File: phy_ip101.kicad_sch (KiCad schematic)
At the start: 36 parts, among them SW1 SW_Push, SW2 SW_Push, U3 ESP32-WROOM-32D, U4 IP101GRI

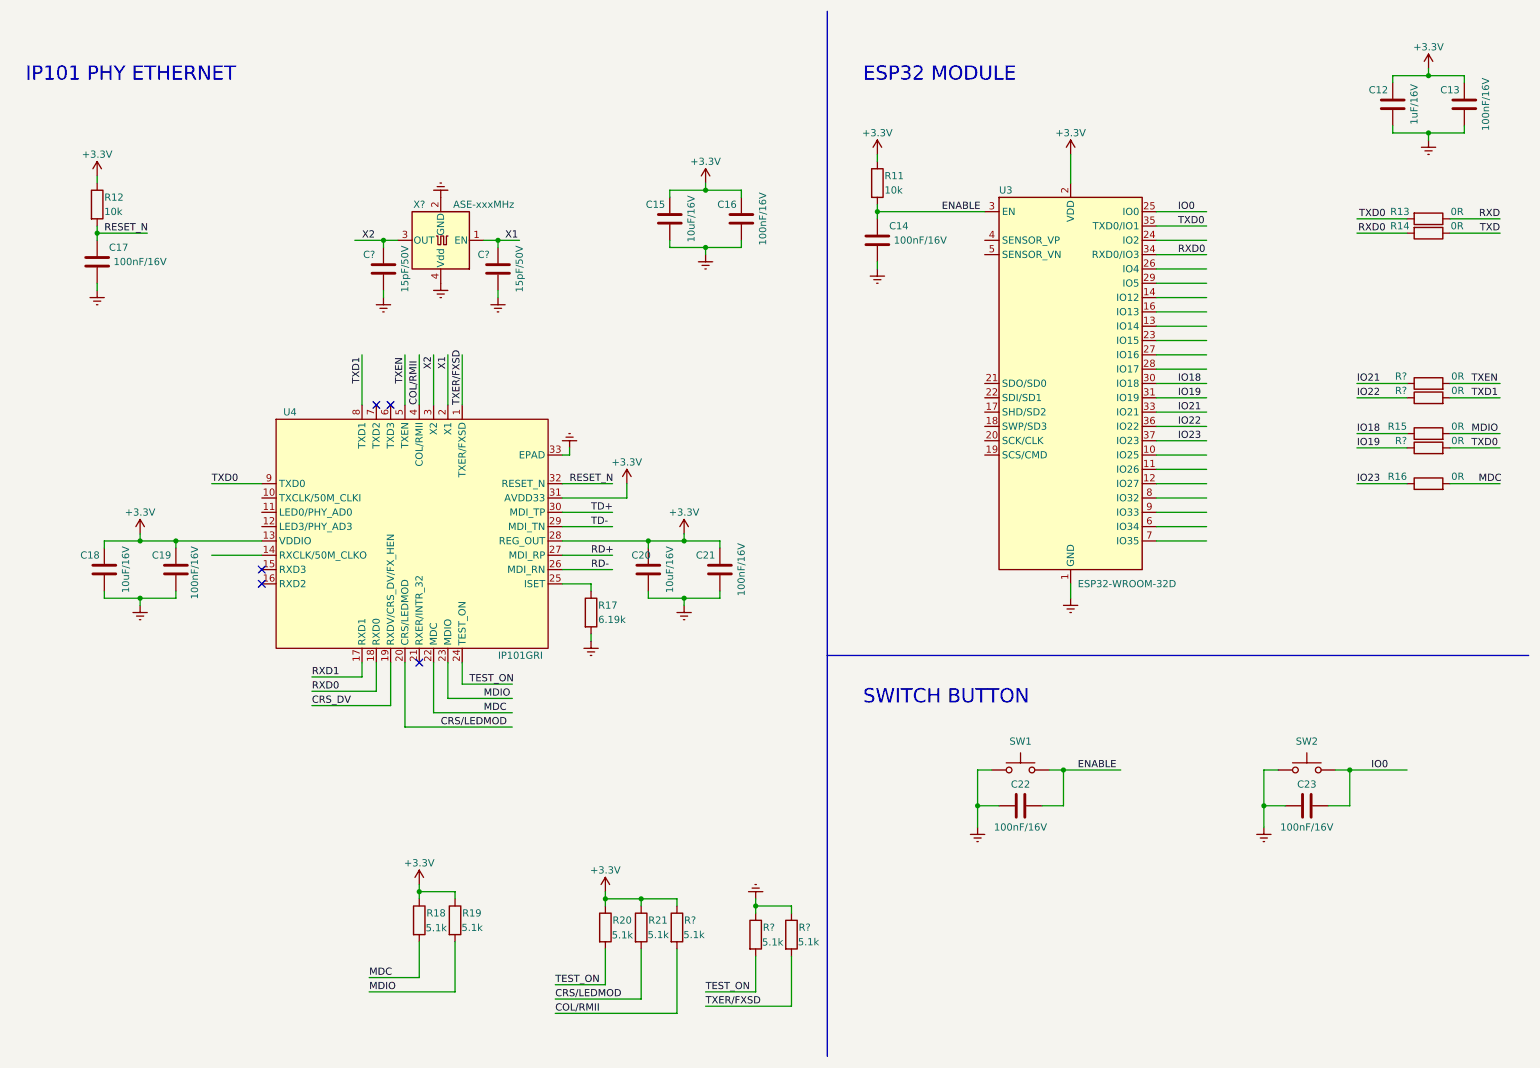
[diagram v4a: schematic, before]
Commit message: Concluido o circuito do PHY ETH
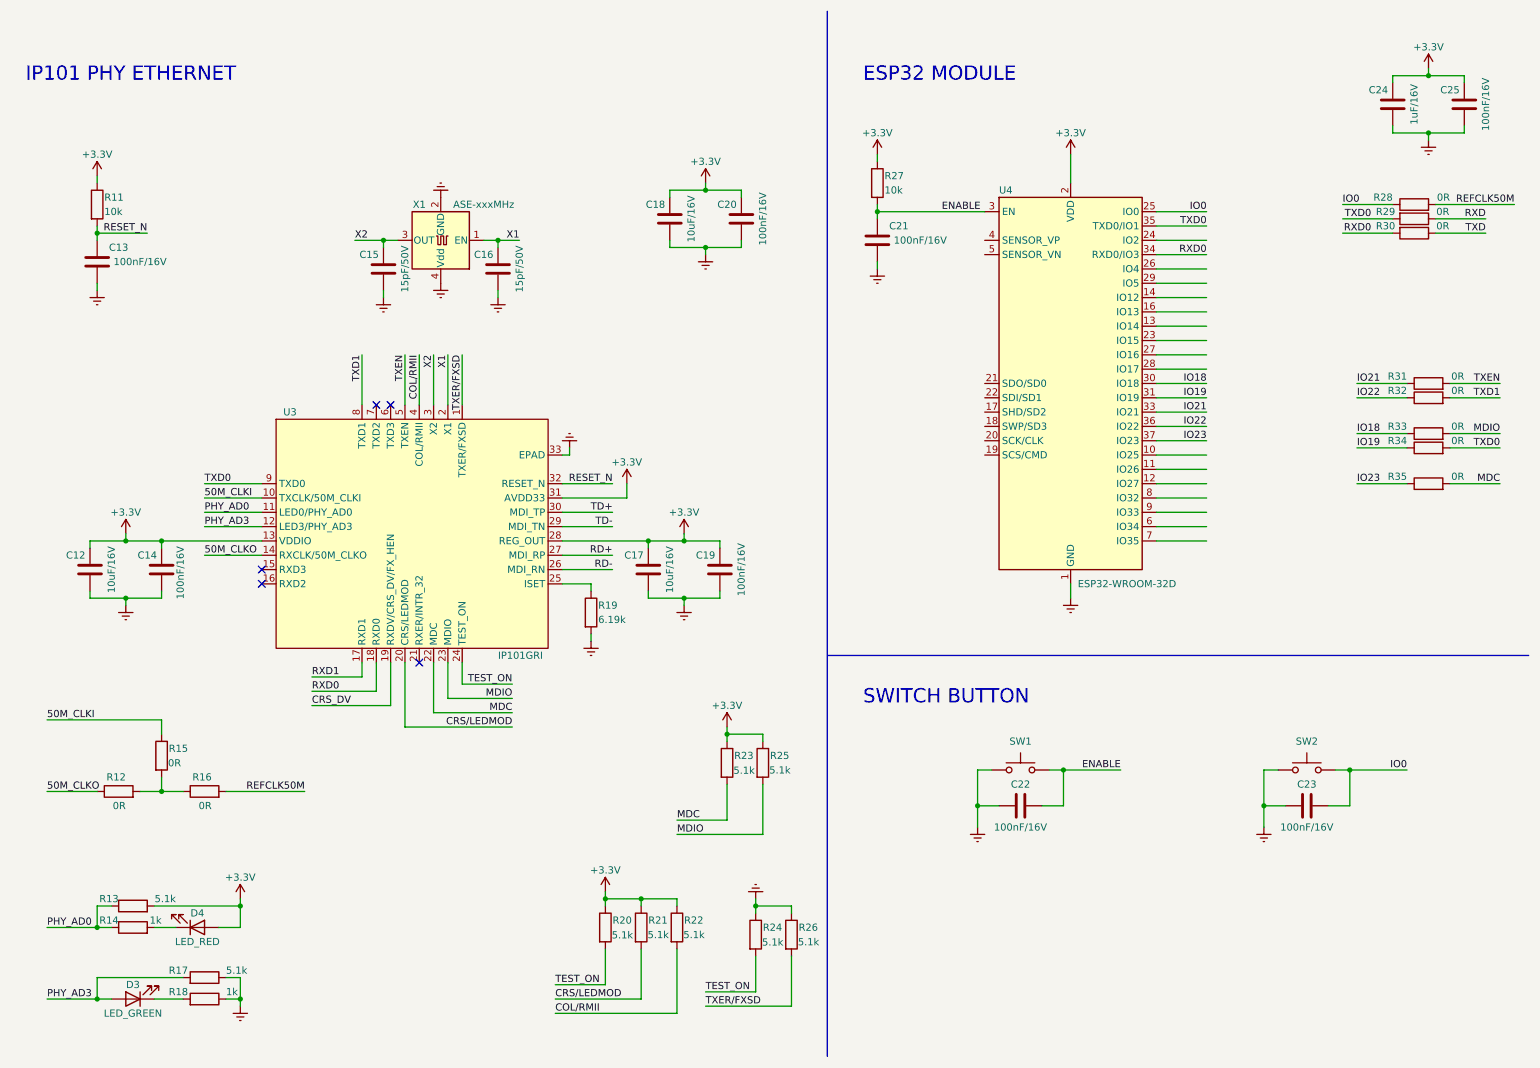
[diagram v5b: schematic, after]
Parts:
- added D3: LED_GREEN, LED_SMD:LED_0603_1608Metric_Pad1.05x0.95mm_HandSolder, symbol Device:LED
- added D4: LED_RED, LED_SMD:LED_0603_1608Metric_Pad1.05x0.95mm_HandSolder, symbol Device:LED
- added R12, R15, R16, R28: 0R, Resistor_SMD:R_0402_1005Metric_Pad0.72x0.64mm_HandSolder, symbol Device:R
- added R13, R17: 5.1k, Resistor_SMD:R_0402_1005Metric_Pad0.72x0.64mm_HandSolder, symbol Device:R
- added R14, R18: 1k, Resistor_SMD:R_0402_1005Metric_Pad0.72x0.64mm_HandSolder, symbol Device:R
- gave numbers to parts that had none: 9
- renumbered C18 to C12, C17 to C13, C19 to C14, C20 to C17, C15 to C18, C21 to C19, C16 to C20, C14 to C21, C12 to C24, C13 to C25, R12 to R11, R17 to R19, R18 to R23, R19 to R25, R11 to R27, R13 to R29, R14 to R30, R15 to R33, R16 to R35, U4 to U3, U3 to U4
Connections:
- net +3V3: now also D4.2 (A), R13.2
- net GNDREF: now also R17.1, R18.1
- net IO0: now also R28.1
- net 50M_CLKI: now reaches U3.10 (TXCLK/50M_CLKI)
- net 50M_CLKI: now also R15.1
- net PHY_AD0: now reaches U3.11 (LED0/PHY_AD0)
- net PHY_AD0: now also R13.1, R14.1
- net PHY_AD3: now reaches U3.12 (LED3/PHY_AD3)
- net PHY_AD3: now also D3.2 (A), R17.2
- net 50M_CLKO: now reaches U3.14 (RXCLK/50M_CLKO)
- net 50M_CLKO: now also R12.1
- new net: D4.1 (K), R14.2
- new net: R12.2, R15.2, R16.1
- new net: D3.1 (K), R18.2
- new net REFCLK50M: R16.2, R28.2
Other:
- moved on the sheet: C12, C14, R23, R25, R29, R30

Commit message: Iniciando o circuito do conector RJ45
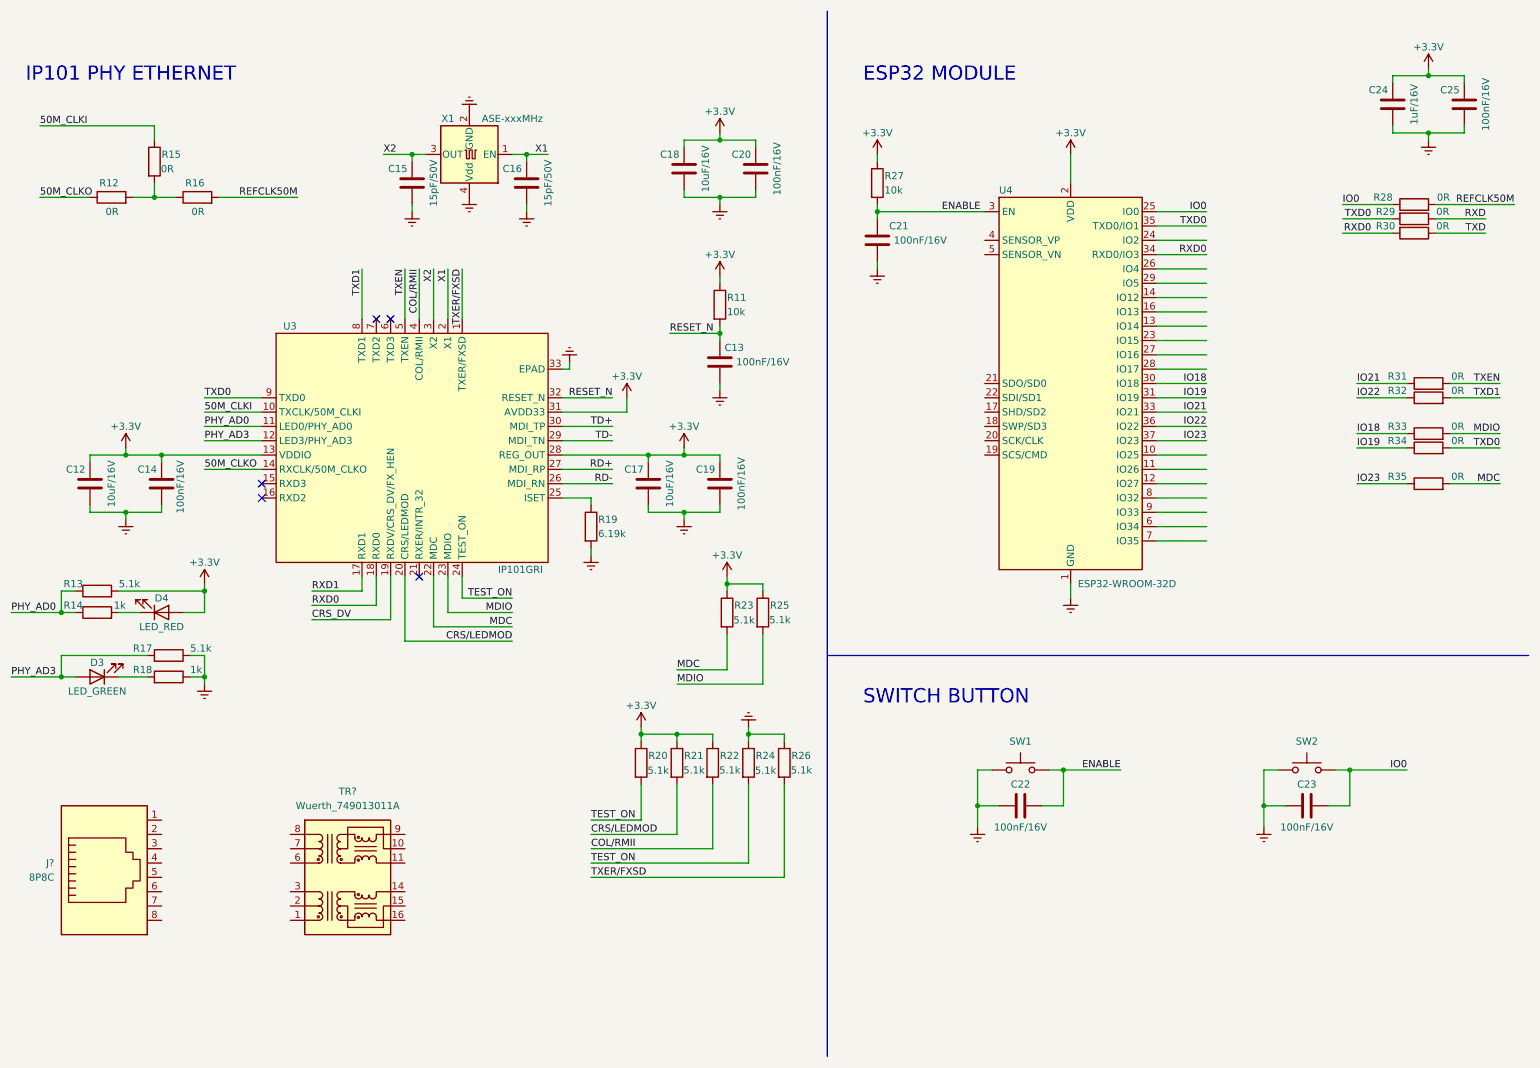
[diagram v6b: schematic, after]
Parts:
- added J?: 8P8C, Transformer_SMD:Transformer_Ethernet_YDS_30F-51NL_SO-24_7.1x15.1mm, symbol Connector:8P8C
- added TR?: Wuerth_749013011A, Transformer_SMD:Transformer_Ethernet_Wuerth_749013011A, symbol Transformer:Wuerth_749013011A
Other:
- moved on the sheet: C12, C13, C14, C15, C16, C17, C18, C19, C20, D3, D4, R11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

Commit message: Criado um sheet para circuito do ESP32
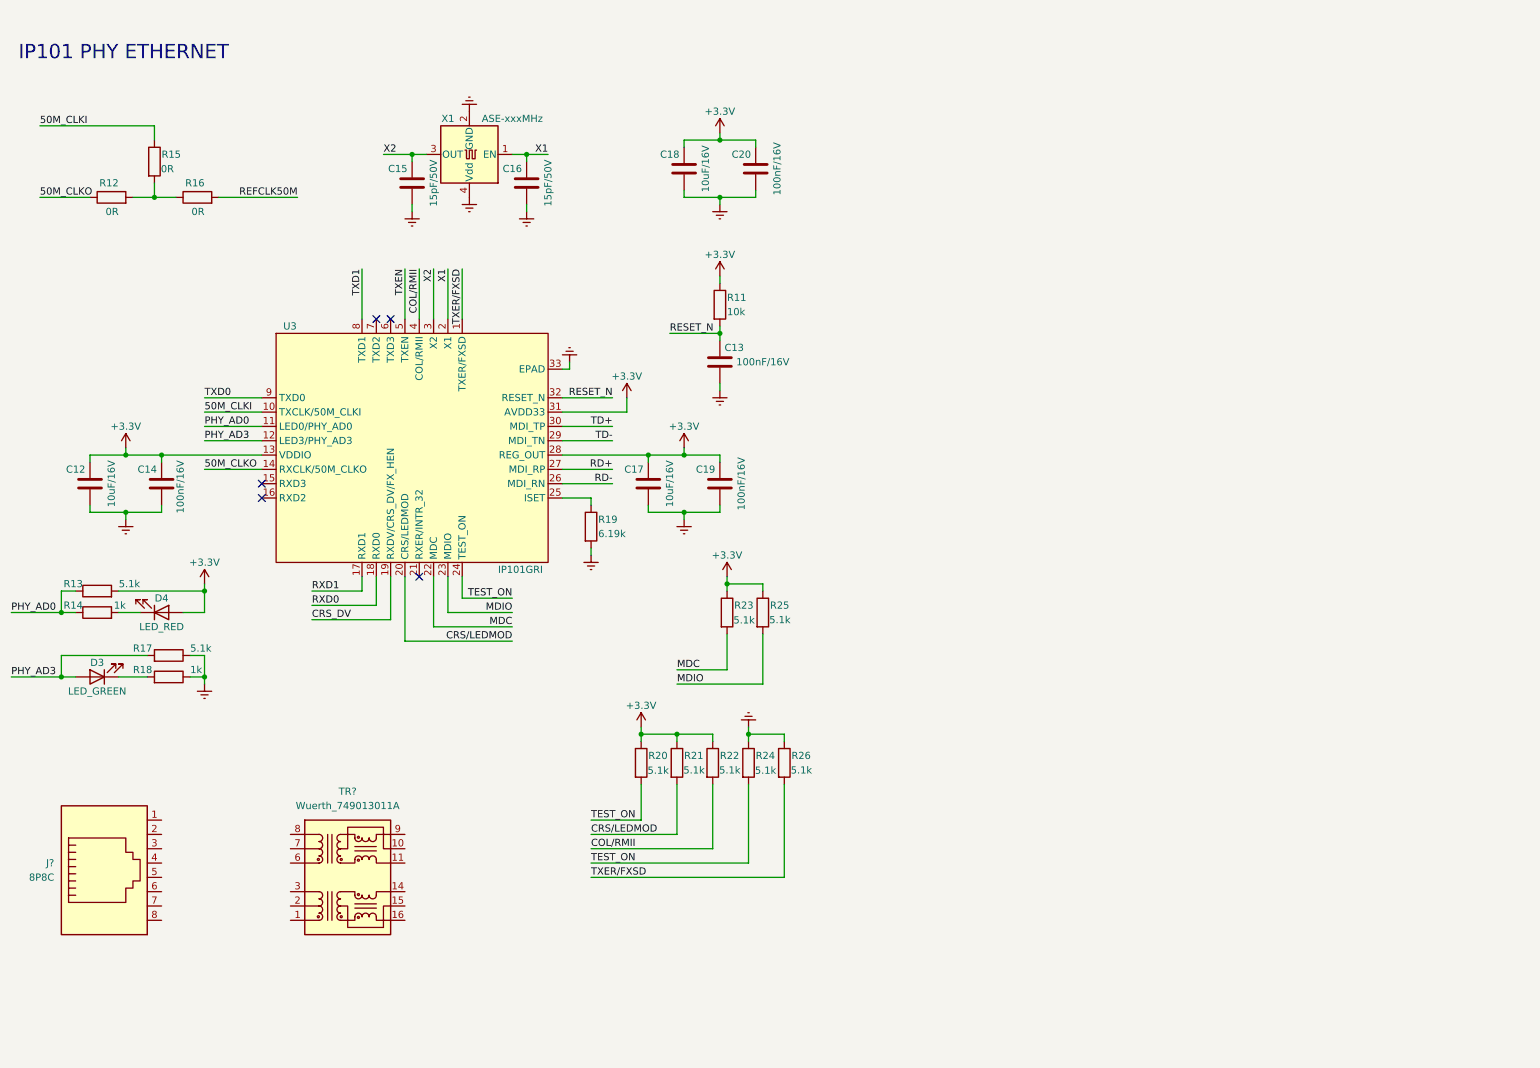
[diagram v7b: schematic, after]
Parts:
- removed C21, C22, C23, C25: 100nF/16V, Capacitor_SMD:C_0402_1005Metric_Pad0.74x0.62mm_HandSolder, symbol Device:C
- removed C24: 1uF/16V, Capacitor_SMD:C_0603_1608Metric_Pad1.08x0.95mm_HandSolder, symbol Device:C
- removed R27: 10k, symbol Device:R
- removed R28, R29, R30, R31, R32, R33, R34, R35: 0R, Resistor_SMD:R_0402_1005Metric_Pad0.72x0.64mm_HandSolder, symbol Device:R
- removed SW1, SW2: SW_Push, Button_Switch_SMD:SW_SPST_CK_RS282G05A3, symbol Switch:SW_Push
- removed U4: ESP32-WROOM-32D, RF_Module:ESP32-WROOM-32, symbol RF_Module:ESP32-WROOM-32D
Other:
- note removed: "ESP32 MODULE"
- note removed: "SWITCH BUTTON"

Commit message: Adicionado o circuito de entrada do PHY ETH
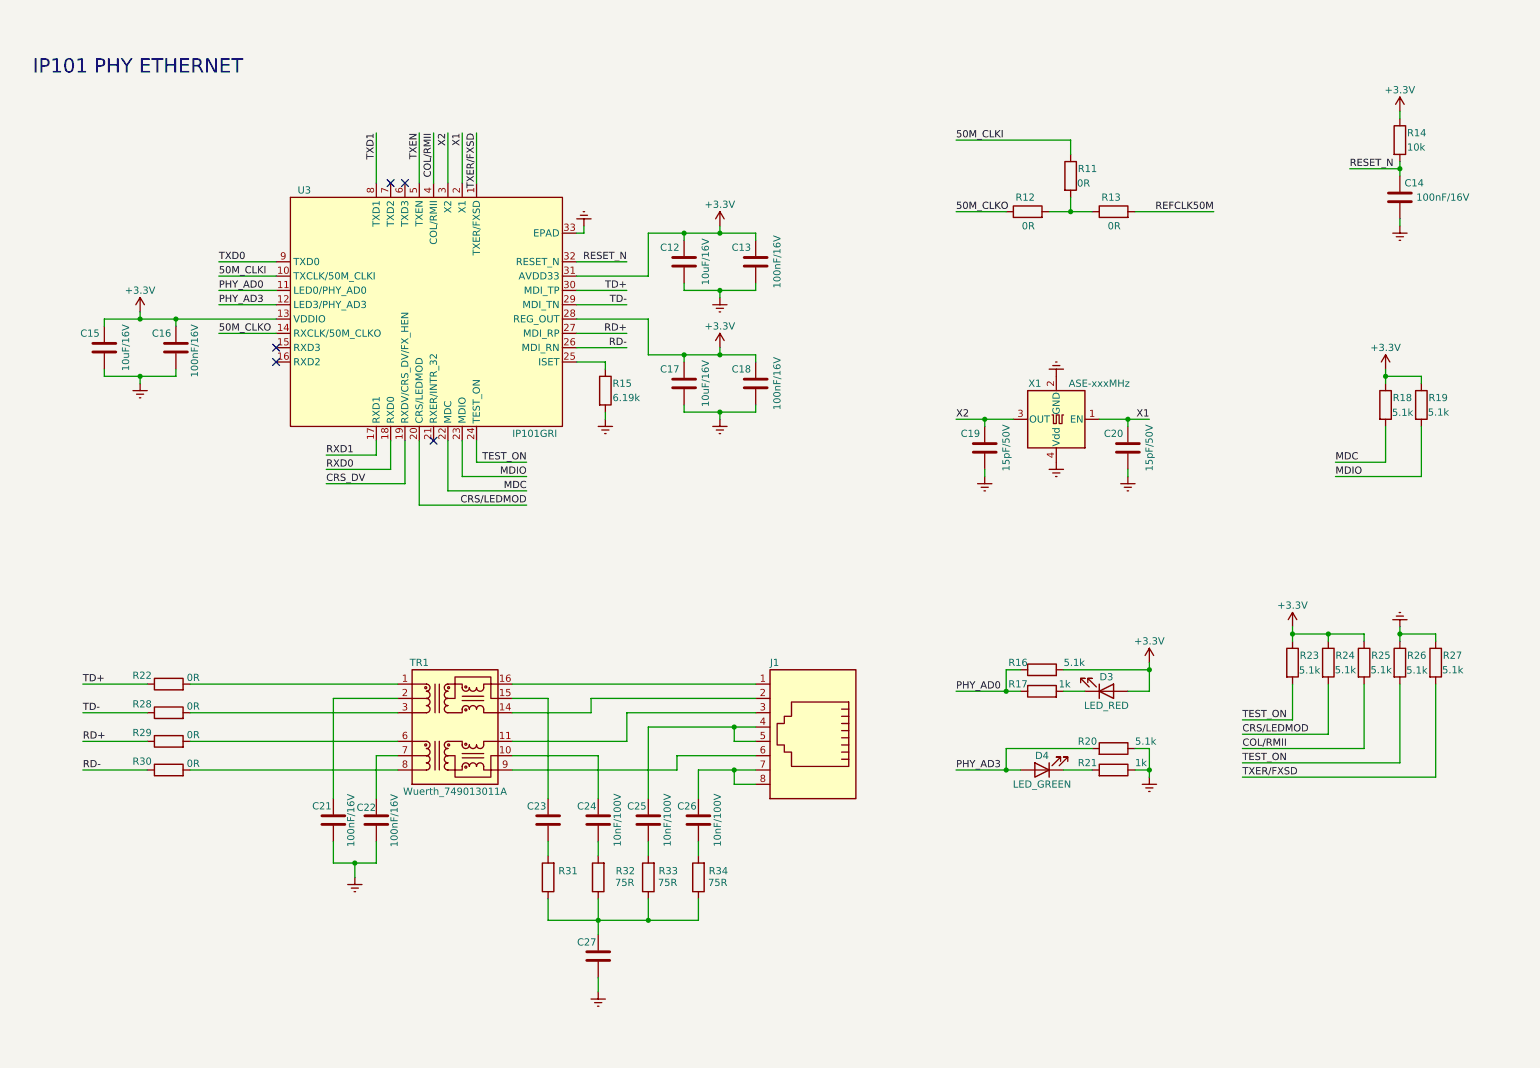
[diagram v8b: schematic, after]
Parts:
- removed J?: 8P8C, Transformer_SMD:Transformer_Ethernet_YDS_30F-51NL_SO-24_7.1x15.1mm, symbol Connector:8P8C
- added C21, C22: 100nF/16V, Capacitor_SMD:C_0402_1005Metric_Pad0.74x0.62mm_HandSolder, symbol Device:C
- added C23: (no value), Capacitor_SMD:C_0402_1005Metric_Pad0.74x0.62mm_HandSolder, symbol Device:C
- added C24, C25, C26: 10nF/100V, Capacitor_SMD:C_0402_1005Metric_Pad0.74x0.62mm_HandSolder, symbol Device:C
- added C27: (no value), symbol Device:C
- added J1: (no value), symbol Connector:8P8C
- added R22, R28, R29, R30: 0R, Resistor_SMD:R_0402_1005Metric_Pad0.72x0.64mm_HandSolder, symbol Device:R
- added R31: (no value), symbol Device:R
- added R32, R33, R34: 75R, Resistor_SMD:R_0402_1005Metric_Pad0.72x0.64mm_HandSolder, symbol Device:R
- gave numbers to parts that had none: 1
- renumbered C18 to C12, C20 to C13, C13 to C14, C12 to C15, C14 to C16, C19 to C18, C15 to C19, C16 to C20, D4 to D3, D3 to D4, R15 to R11, R16 to R13, R11 to R14, R19 to R15, R13 to R16, R14 to R17, R23 to R18, R25 to R19, R17 to R20, R18 to R21, R20 to R23, R21 to R24, R22 to R25, R24 to R26, R26 to R27
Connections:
- net GNDREF: now also C21.1, C22.1, C27.1
- net RD+: now also R29.1
- net RD-: now also R30.1
- net TD+: now also R22.1
- net TD-: now also R28.1
- net at TR1.1 (TD+): now also R22.2
- net at TR1.10 (C_RX): now also C24.2
- net at TR1.11 (RX+): now also J1.3
- net at TR1.14 (TX-): now also J1.2
- net at TR1.15 (C_TX): now also C23.2
- net at TR1.16 (TX+): now also J1.1
- net at TR1.2 (C_TD): now also C21.2
- net at TR1.3 (TD-): now also R28.2
- net at TR1.6 (RD+): now also R29.2
- net at TR1.7 (C_RD): now also C22.2
- net at TR1.8 (RD-): now also R30.2
- net at TR1.9 (RX-): now also J1.6
- new net: C26.1, R34.2
- new net: C26.2, J1.7, J1.8
- new net: C27.2, R31.1, R32.1, R33.1, R34.1
- new net: C23.1, R31.2
- new net: C25.2, J1.4, J1.5
- new net: C25.1, R33.2
- new net: C24.1, R32.2
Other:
- moved on the sheet: C12, C13, C14, C15, C16, C17, C18, C19, C20, D3, D4, R11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
